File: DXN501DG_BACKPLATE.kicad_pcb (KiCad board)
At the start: 2 copper layers, 170 x 130 mm, 4 parts

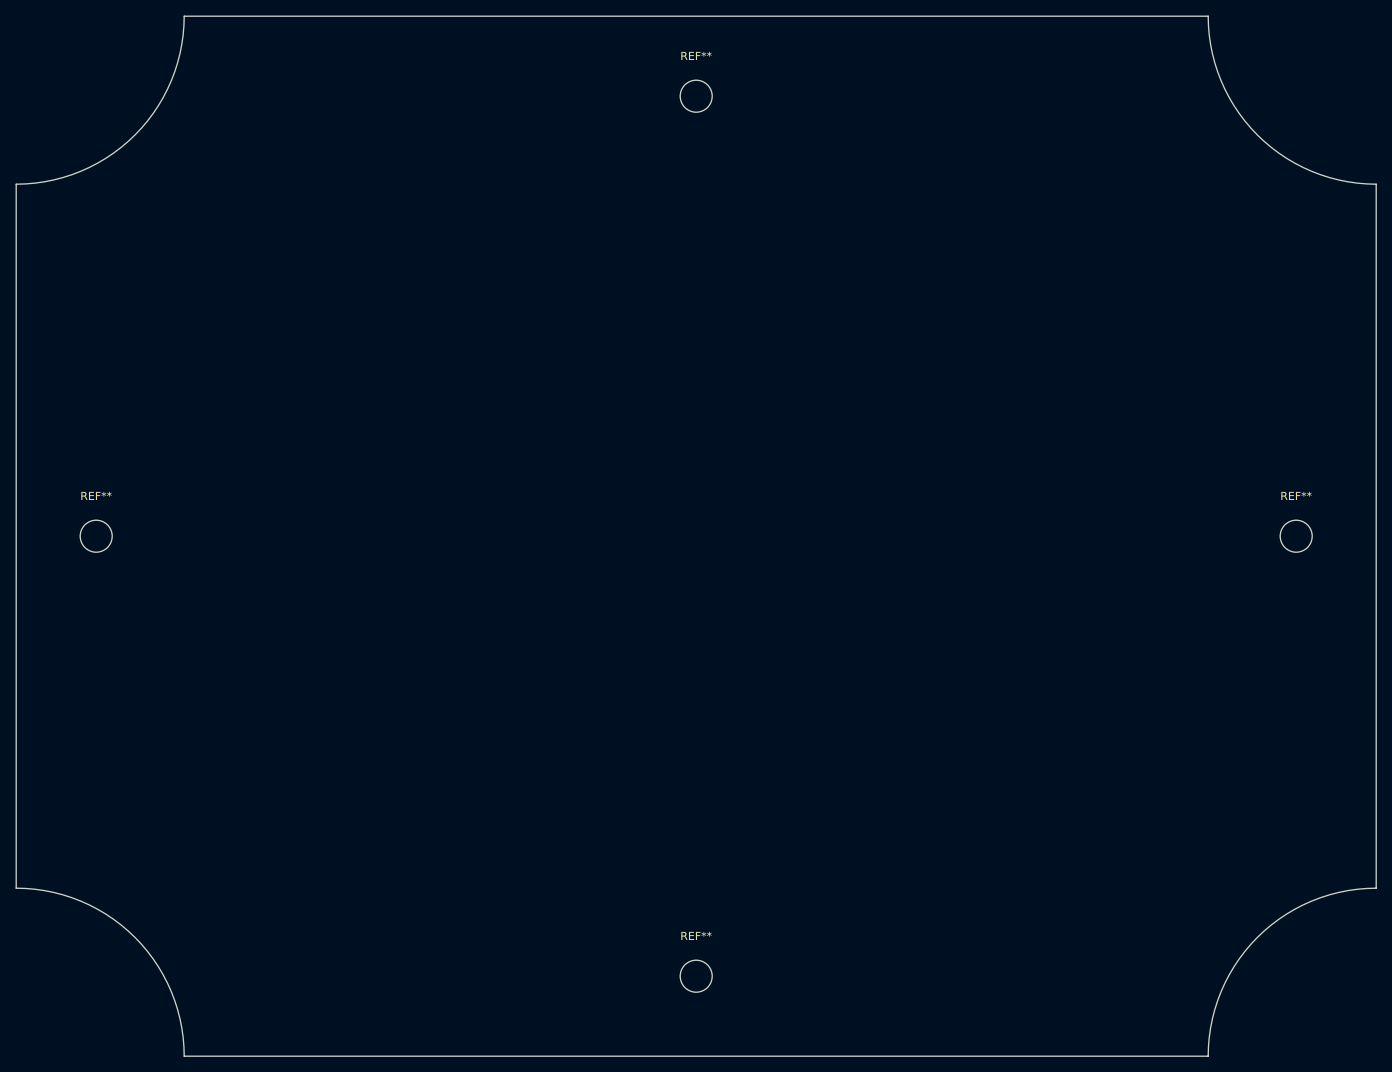
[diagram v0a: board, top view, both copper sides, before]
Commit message: changed drills for circles
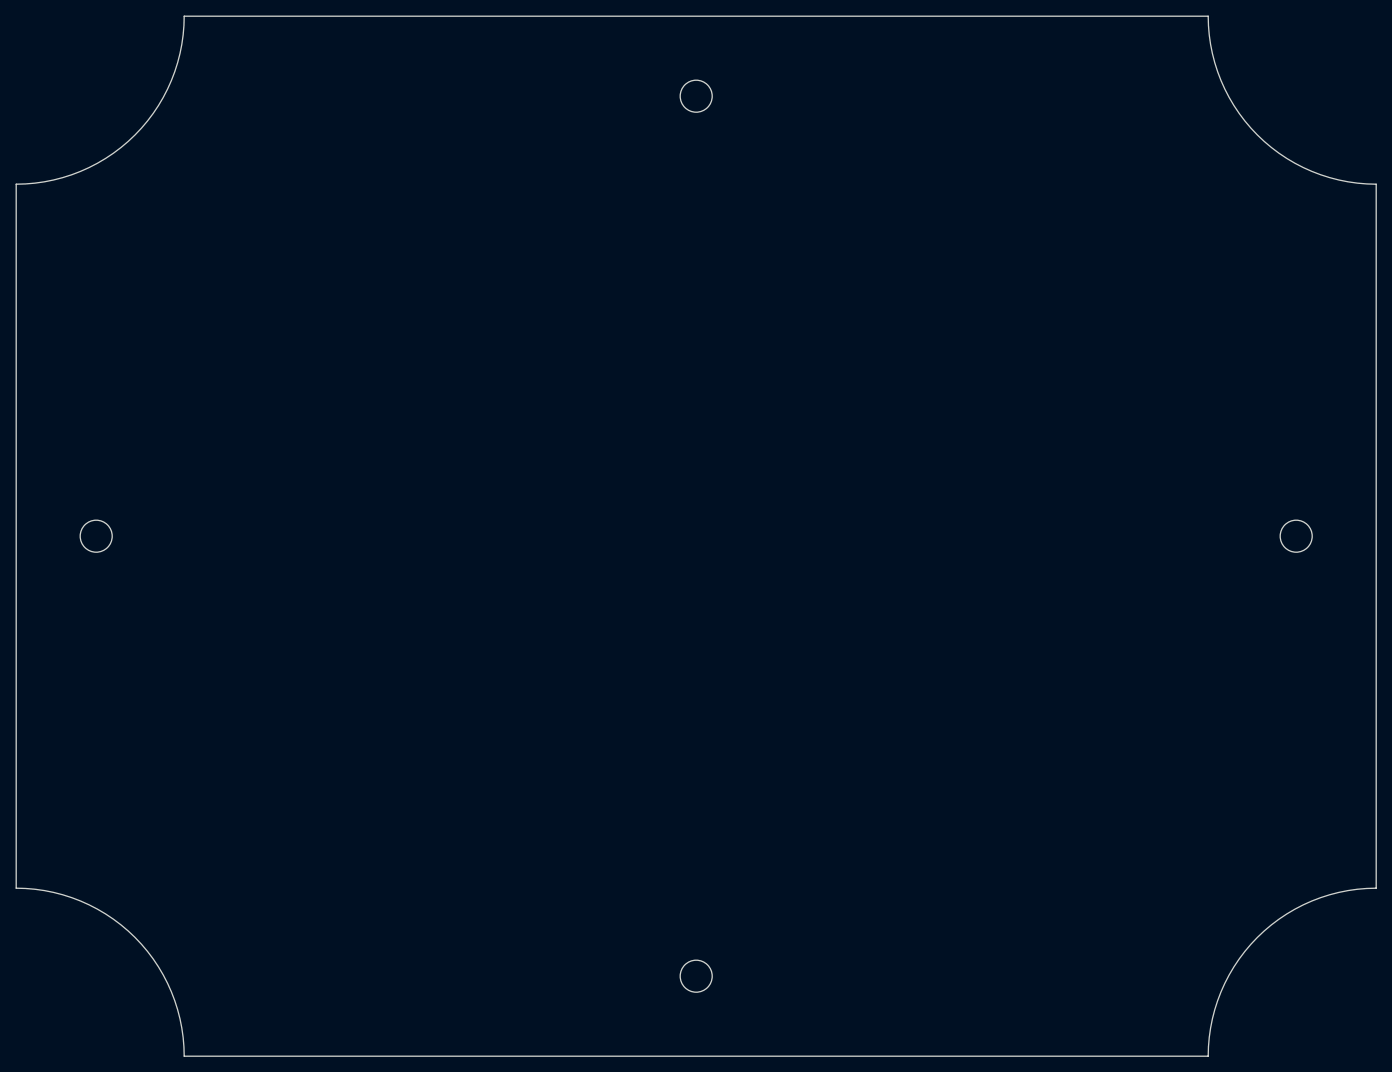
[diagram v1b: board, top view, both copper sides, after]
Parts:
- removed REF** (x4): MountingHole_4mm, MountingHole:MountingHole_4mm
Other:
- outline, holes or cut-outs redrawn
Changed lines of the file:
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@@
   (general
     (thickness 1.6)
-    (drawings 8)
+    (drawings 12)
     (tracks 0)
     (zones 0)
-    (modules 4)
+    (modules 0)
     (nets 1)
   )
@@
     (visible_elements FFFFFF7F)
     (pcbplotparams
-      (layerselection 0x010fc_ffffffff)
+      (layerselection 0x01000_7ffffffe)
       (usegerberextensions false)
       (usegerberattributes false)
@@
       (padsonsilk false)
       (subtractmaskfromsilk false)
-      (outputformat 1)
+      (outputformat 5)
       (mirror false)
-      (drillshape 1)
+      (drillshape 2)
       (scaleselection 1)
-      (outputdirectory ""))
+      (outputdirectory "dxf/"))
   )
   (net 0 "")
@@
     (uvia_drill 0.1)
   )
-  (module MountingHole:MountingHole_4mm (layer F.Cu)
-    (at 105 140)
-    (descr "Mounting Hole 4mm, no annular")
-    (tags "mounting hole 4mm no annular")
-    (attr virtual)
-    (fp_text reference REF** (at 0 -5) (layer F.SilkS)
-      (effects (font (size 1 1) (thickness 0.15)))
-    )
-    (fp_text value MountingHole_4mm (at 0 5) (layer F.Fab)
-      (effects (font (size 1 1) (thickness 0.15)))
-    )
-    (fp_circle (center 0 0) (end 4.25 0) (layer F.CrtYd) (width 0.05))
-    (fp_circle (center 0 0) (end 4 0) (layer Cmts.User) (width 0.15))
-    (fp_text user %R (at 0.3 0) (layer F.Fab)
-      (effects (font (size 1 1) (thickness 0.15)))
-    )
-    (pad 1 np_thru_hole circle (at 0 0) (size 4 4) (drill 4) (layers *.Cu *.Mask))
-  )
-  (module MountingHole:MountingHole_4mm (layer F.Cu)
-    (at 105 30)
-    (descr "Mounting Hole 4mm, no annular")
-    (tags "mounting hole 4mm no annular")
-    (attr virtual)
-    (fp_text reference REF** (at 0 -5) (layer F.SilkS)
-      (effects (font (size 1 1) (thickness 0.15)))
-    )
-    (fp_text value MountingHole_4mm (at 0 5) (layer F.Fab)
-      (effects (font (size 1 1) (thickness 0.15)))
-    )
-    (fp_circle (center 0 0) (end 4.25 0) (layer F.CrtYd) (width 0.05))
-    (fp_circle (center 0 0) (end 4 0) (layer Cmts.User) (width 0.15))
-    (fp_text user %R (at 0.3 0) (layer F.Fab)
-      (effects (font (size 1 1) (thickness 0.15)))
-    )
-    (pad 1 np_thru_hole circle (at 0 0) (size 4 4) (drill 4) (layers *.Cu *.Mask))
-  )
-  (module MountingHole:MountingHole_4mm (layer F.Cu)
-    (at 180 85)
-    (descr "Mounting Hole 4mm, no annular")
-    (tags "mounting hole 4mm no annular")
-    (attr virtual)
-    (fp_text reference REF** (at 0 -5) (layer F.SilkS)
-      (effects (font (size 1 1) (thickness 0.15)))
-    )
-    (fp_text value MountingHole_4mm (at 0 5) (layer F.Fab)
-      (effects (font (size 1 1) (thickness 0.15)))
-    )
-    (fp_circle (center 0 0) (end 4.25 0) (layer F.CrtYd) (width 0.05))
-    (fp_circle (center 0 0) (end 4 0) (layer Cmts.User) (width 0.15))
-    (fp_text user %R (at 0.3 0) (layer F.Fab)
-      (effects (font (size 1 1) (thickness 0.15)))
-    )
-    (pad 1 np_thru_hole circle (at 0 0) (size 4 4) (drill 4) (layers *.Cu *.Mask))
-  )
-  (module MountingHole:MountingHole_4mm (layer F.Cu)
-    (at 30 85)
-    (descr "Mounting Hole 4mm, no annular")
-    (tags "mounting hole 4mm no annular")
-    (attr virtual)
-    (fp_text reference REF** (at 0 -5) (layer F.SilkS)
-      (effects (font (size 1 1) (thickness 0.15)))
-    )
-    (fp_text value MountingHole_4mm (at 0 5) (layer F.Fab)
-      (effects (font (size 1 1) (thickness 0.15)))
-    )
-    (fp_circle (center 0 0) (end 4.25 0) (layer F.CrtYd) (width 0.05))
-    (fp_circle (center 0 0) (end 4 0) (layer Cmts.User) (width 0.15))
-    (fp_text user %R (at 0.3 0) (layer F.Fab)
-      (effects (font (size 1 1) (thickness 0.15)))
-    )
-    (pad 1 np_thru_hole circle (at 0 0) (size 4 4) (drill 4) (layers *.Cu *.Mask))
-  )
+  (gr_circle (center 30 85) (end 32 85) (layer Edge.Cuts) (width 0.05))
+  (gr_circle (center 105 30) (end 107 30) (layer Edge.Cuts) (width 0.05))
+  (gr_circle (center 180 85) (end 182 85) (layer Edge.Cuts) (width 0.05))
+  (gr_circle (center 105 140) (end 107 140) (layer Edge.Cuts) (width 0.05))
   (gr_arc (start 190 150) (end 190 129) (angle -90) (layer Edge.Cuts) (width 0.05))
   (gr_arc (start 190 20) (end 169 20) (angle -90) (layer Edge.Cuts) (width 0.05))
